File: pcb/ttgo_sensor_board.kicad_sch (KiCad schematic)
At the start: 59 parts, among them J1 Conn_01x13_Female, J2 Conn_01x13_Female, J3 Conn_01x03_Female, J4 Conn_01x03_Female, J5 Conn_01x04_Female, J6 Conn_01x04_Female, J7 Conn_01x04_Female, Q1 Q_NMOS_GSD, Q2 Q_NMOS_GSD, U1 BME680, U2 TCA9800, U3 TLV70218_SOT23-5, U4 LSM6DS3, U5 VEML7700

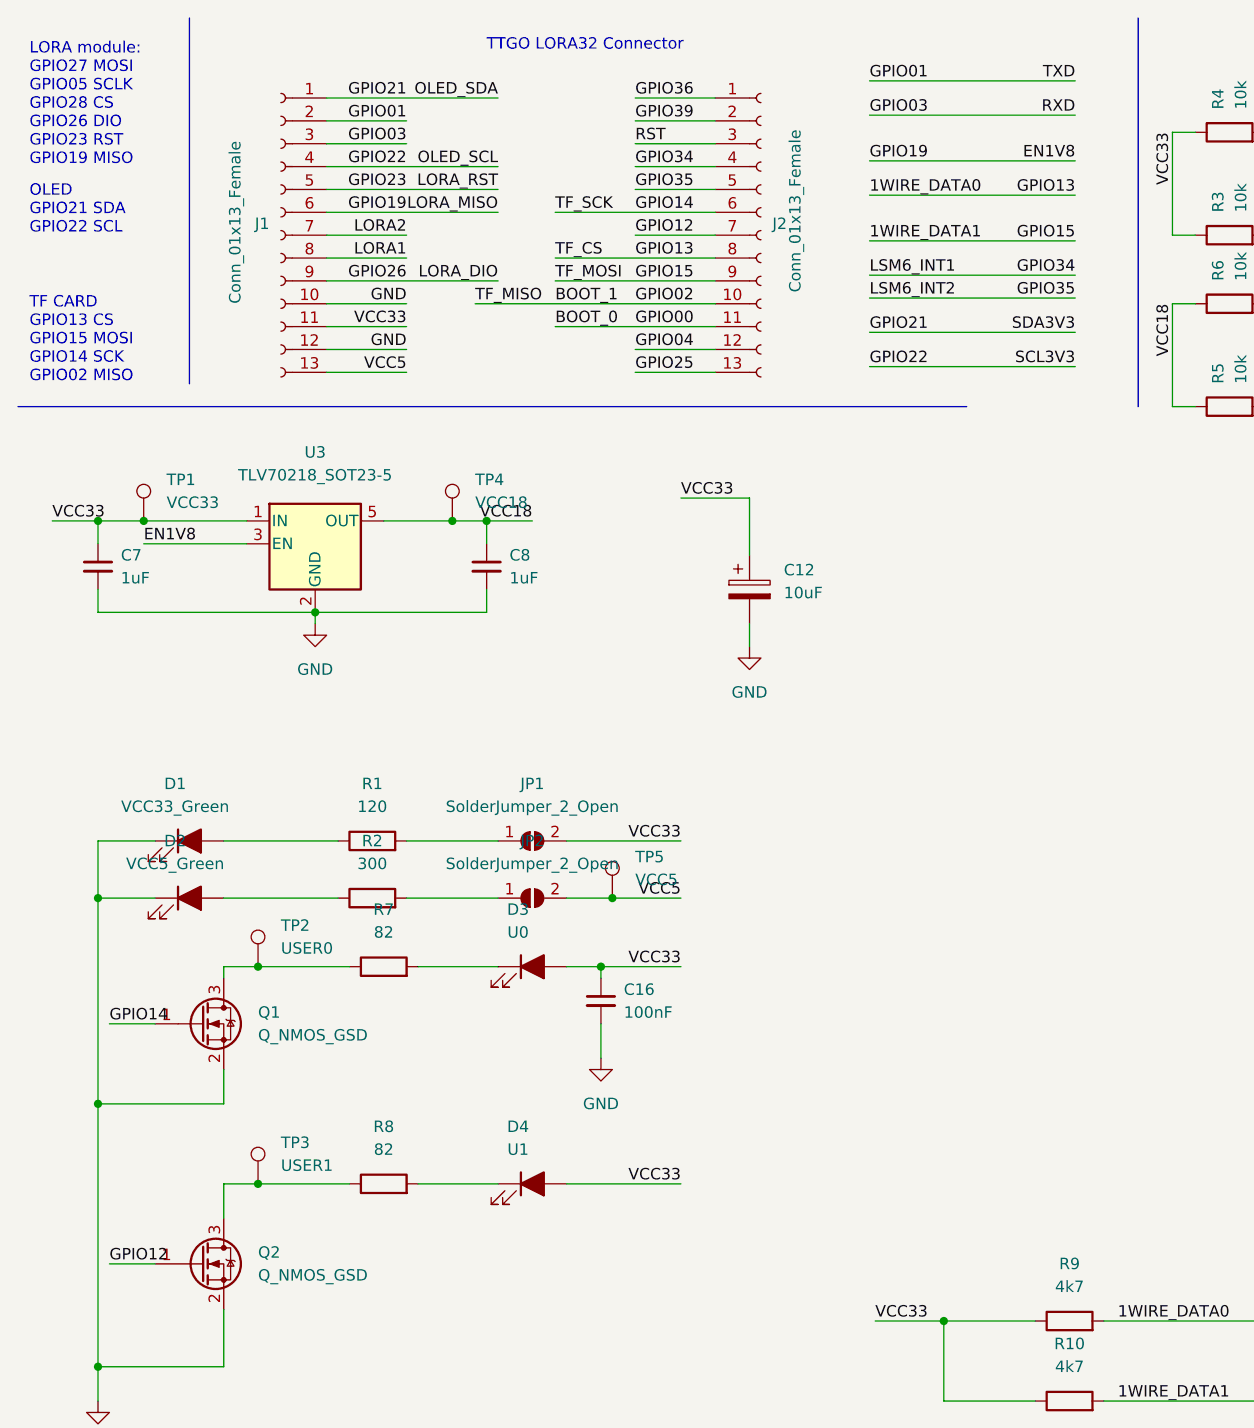
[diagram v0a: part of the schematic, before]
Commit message: update schematic
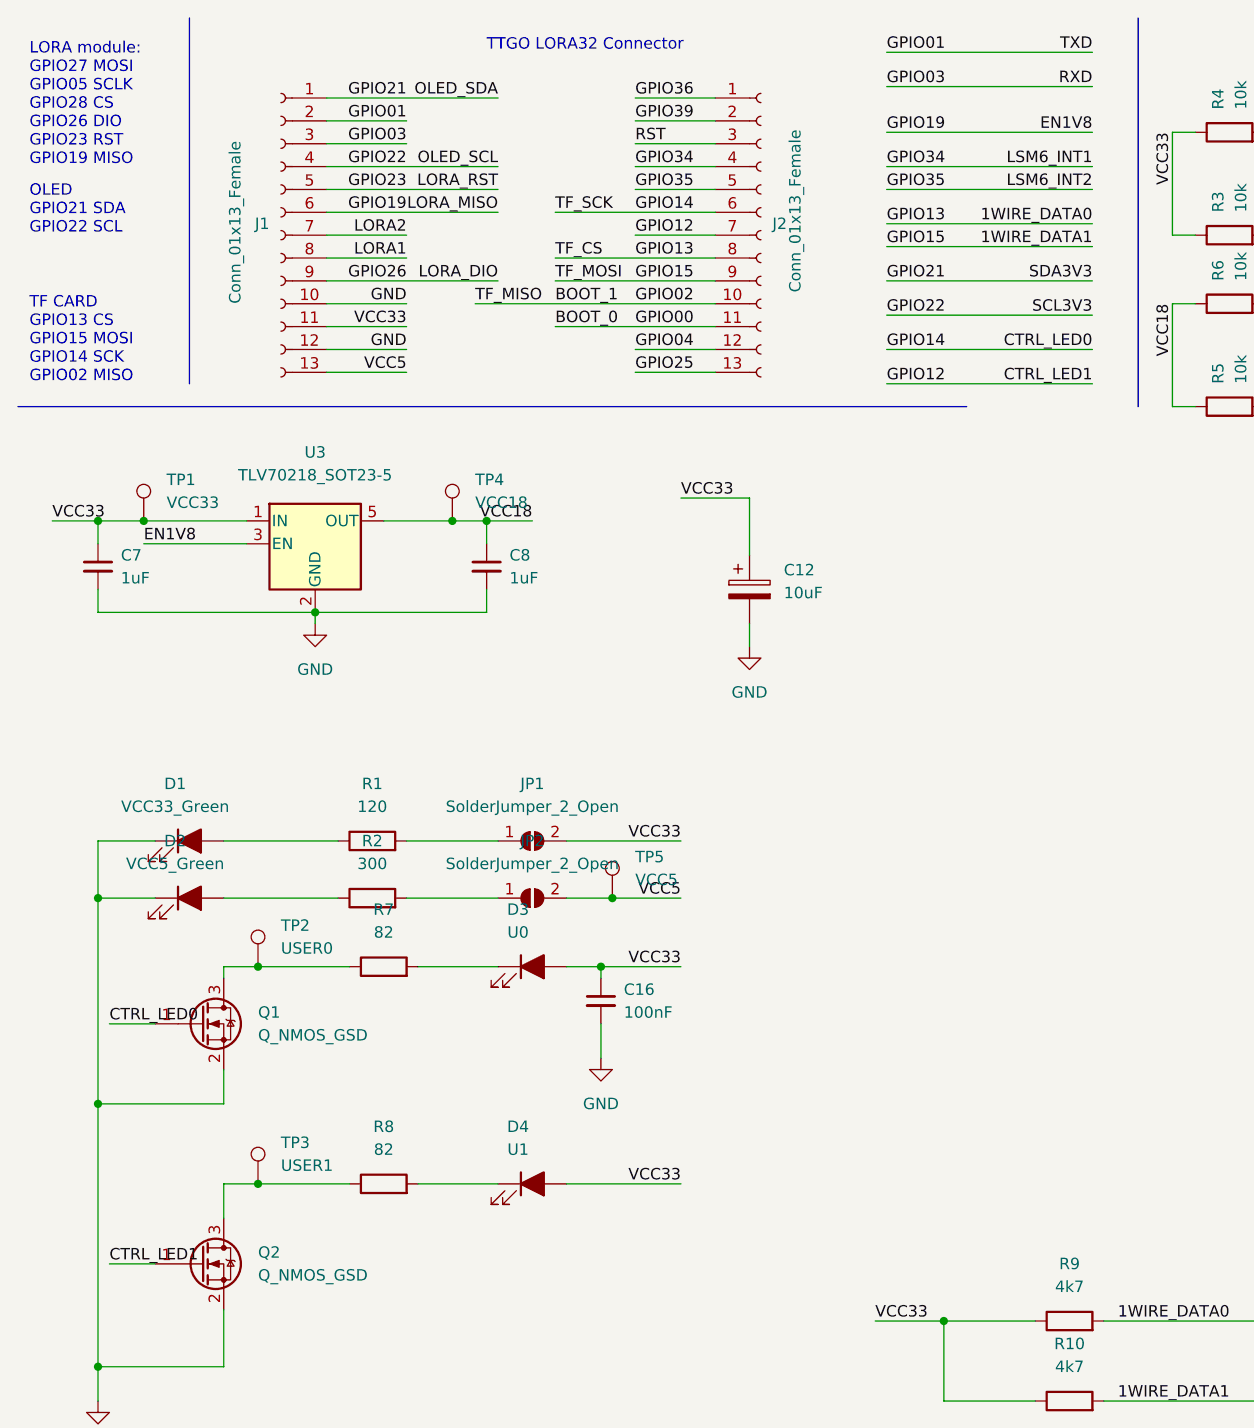
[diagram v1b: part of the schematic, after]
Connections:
- net GPIO12 renamed CTRL_LED1
- net GPIO14 renamed CTRL_LED0
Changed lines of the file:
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@@
     (stroke (width 0) (type default))
   )
-  (wire (pts (xy 108.585 32.385) (xy 131.445 32.385))
+  (wire (pts (xy 133.35 35.56) (xy 110.49 35.56))
+    (stroke (width 0) (type default))
+  )
+  (wire (pts (xy 110.49 49.53) (xy 133.35 49.53))
     (stroke (width 0) (type default))
   )
@@
     (stroke (width 0) (type default))
   )
-  (wire (pts (xy 108.585 41.275) (xy 131.445 41.275))
+  (wire (pts (xy 133.35 29.21) (xy 110.49 29.21))
     (stroke (width 0) (type default))
   )
@@
     (stroke (width 0) (type default))
   )
+  (wire (pts (xy 110.49 53.34) (xy 133.35 53.34))
+    (stroke (width 0) (type default))
+  )
   (wire (pts (xy 22.86 104.14) (xy 22.86 110.49))
     (stroke (width 0) (type default))
@@
     (stroke (width 0) (type default))
   )
-  (wire (pts (xy 108.585 47.625) (xy 131.445 47.625))
+  (wire (pts (xy 110.49 41.91) (xy 133.35 41.91))
     (stroke (width 0) (type default))
   )
@@
     (stroke (width 0) (type default))
   )
-  (wire (pts (xy 108.585 23.495) (xy 131.445 23.495))
+  (wire (pts (xy 110.49 20.32) (xy 133.35 20.32))
     (stroke (width 0) (type default))
   )
@@
     (stroke (width 0) (type default))
   )
-  (wire (pts (xy 108.585 19.685) (xy 131.445 19.685))
+  (wire (pts (xy 110.49 16.51) (xy 133.35 16.51))
     (stroke (width 0) (type default))
   )
@@
     (stroke (width 0) (type default))
   )
-  (wire (pts (xy 108.585 51.435) (xy 131.445 51.435))
+  (wire (pts (xy 110.49 45.72) (xy 133.35 45.72))
     (stroke (width 0) (type default))
   )
@@
     (stroke (width 0) (type default))
   )
-  (wire (pts (xy 108.585 37.465) (xy 131.445 37.465))
+  (wire (pts (xy 133.35 38.1) (xy 110.49 38.1))
     (stroke (width 0) (type default))
   )
@@
     (stroke (width 0) (type default))
   )
-  (wire (pts (xy 108.585 28.575) (xy 131.445 28.575))
+  (wire (pts (xy 110.49 25.4) (xy 133.35 25.4))
     (stroke (width 0) (type default))
   )
@@
     (stroke (width 0) (type default))
   )
-  (wire (pts (xy 108.585 43.815) (xy 131.445 43.815))
+  (wire (pts (xy 133.35 31.75) (xy 110.49 31.75))
     (stroke (width 0) (type default))
   )
@@
     (effects (font (size 1.27 1.27)) (justify left bottom))
   )
-  (label "1WIRE_DATA1" (at 108.585 37.465 0) (fields_autoplaced)
-    (effects (font (size 1.27 1.27)) (justify left bottom))
+  (label "1WIRE_DATA1" (at 133.35 38.1 180) (fields_autoplaced)
+    (effects (font (size 1.27 1.27)) (justify right bottom))
   )
   (label "GPIO14" (at 82.55 34.29 0) (fields_autoplaced)
@@
     (effects (font (size 1.27 1.27)) (justify right bottom))
   )
+  (label "GPIO14" (at 110.49 49.53 0) (fields_autoplaced)
+    (effects (font (size 1.27 1.27)) (justify left bottom))
+  )
   (label "SDA3V3" (at 161.29 36.83 180) (fields_autoplaced)
     (effects (font (size 1.27 1.27)) (justify right bottom))
@@
     (effects (font (size 1.27 1.27)) (justify right bottom))
   )
-  (label "LSM6_INT2" (at 108.585 43.815 0) (fields_autoplaced)
-    (effects (font (size 1.27 1.27)) (justify left bottom))
+  (label "LSM6_INT2" (at 133.35 31.75 180) (fields_autoplaced)
+    (effects (font (size 1.27 1.27)) (justify right bottom))
   )
   (label "GPIO22" (at 57.15 29.21 180) (fields_autoplaced)
     (effects (font (size 1.27 1.27)) (justify right bottom))
   )
-  (label "TXD" (at 131.445 19.685 180) (fields_autoplaced)
+  (label "TXD" (at 133.35 16.51 180) (fields_autoplaced)
     (effects (font (size 1.27 1.27)) (justify right bottom))
   )
@@
     (effects (font (size 1.27 1.27)) (justify left bottom))
   )
-  (label "GPIO03" (at 108.585 23.495 0) (fields_autoplaced)
-    (effects (font (size 1.27 1.27)) (justify left bottom))
-  )
-  (label "GPIO34" (at 131.445 41.275 180) (fields_autoplaced)
-    (effects (font (size 1.27 1.27)) (justify right bottom))
+  (label "CTRL_LED1" (at 133.35 53.34 180) (fields_autoplaced)
+    (effects (font (size 1.27 1.27)) (justify right bottom))
+  )
+  (label "GPIO03" (at 110.49 20.32 0) (fields_autoplaced)
+    (effects (font (size 1.27 1.27)) (justify left bottom))
+  )
+  (label "GPIO34" (at 110.49 29.21 0) (fields_autoplaced)
+    (effects (font (size 1.27 1.27)) (justify left bottom))
   )
   (label "VCC33" (at 17.78 68.58 0) (fields_autoplaced)
@@
     (effects (font (size 1.27 1.27)) (justify left bottom))
   )
+  (label "CTRL_LED0" (at 133.35 49.53 180) (fields_autoplaced)
+    (effects (font (size 1.27 1.27)) (justify right bottom))
+  )
   (label "VCC33" (at 213.36 20.32 180) (fields_autoplaced)
     (effects (font (size 1.27 1.27)) (justify right bottom))
@@
     (effects (font (size 1.27 1.27)) (justify right bottom))
   )
-  (label "1WIRE_DATA0" (at 108.585 32.385 0) (fields_autoplaced)
-    (effects (font (size 1.27 1.27)) (justify left bottom))
+  (label "1WIRE_DATA0" (at 133.35 35.56 180) (fields_autoplaced)
+    (effects (font (size 1.27 1.27)) (justify right bottom))
   )
   (label "GPIO39" (at 82.55 24.13 0) (fields_autoplaced)
     (effects (font (size 1.27 1.27)) (justify left bottom))
   )
-  (label "GPIO13" (at 131.445 32.385 180) (fields_autoplaced)
-    (effects (font (size 1.27 1.27)) (justify right bottom))
+  (label "GPIO13" (at 110.49 35.56 0) (fields_autoplaced)
+    (effects (font (size 1.27 1.27)) (justify left bottom))
   )
   (label "VCC18" (at 71.12 68.58 180) (fields_autoplaced)
@@
     (effects (font (size 1.27 1.27)) (justify left bottom))
   )
-  (label "EN1V8" (at 131.445 28.575 180) (fields_autoplaced)
+  (label "EN1V8" (at 133.35 25.4 180) (fields_autoplaced)
     (effects (font (size 1.27 1.27)) (justify right bottom))
   )
@@
     (effects (font (size 1.27 1.27)) (justify right bottom))
   )
-  (label "SCL3V3" (at 131.445 51.435 180) (fields_autoplaced)
+  (label "SCL3V3" (at 133.35 45.72 180) (fields_autoplaced)
     (effects (font (size 1.27 1.27)) (justify right bottom))
   )
@@
     (effects (font (size 1.27 1.27)) (justify left bottom))
   )
-  (label "GPIO01" (at 108.585 19.685 0) (fields_autoplaced)
+  (label "GPIO01" (at 110.49 16.51 0) (fields_autoplaced)
     (effects (font (size 1.27 1.27)) (justify left bottom))
   )
@@
     (effects (font (size 1.27 1.27)) (justify left bottom))
   )
-  (label "SDA3V3" (at 131.445 47.625 180) (fields_autoplaced)
+  (label "SDA3V3" (at 133.35 41.91 180) (fields_autoplaced)
     (effects (font (size 1.27 1.27)) (justify right bottom))
   )
@@
     (effects (font (size 1.27 1.27)) (justify left bottom))
   )
-  (label "GPIO35" (at 131.445 43.815 180) (fields_autoplaced)
-    (effects (font (size 1.27 1.27)) (justify right bottom))
+  (label "GPIO35" (at 110.49 31.75 0) (fields_autoplaced)
+    (effects (font (size 1.27 1.27)) (justify left bottom))
   )
   (label "LORA_MISO" (at 67.31 34.29 180) (fields_autoplaced)
@@
     (effects (font (size 1.27 1.27)) (justify right bottom))
   )
+  (label "GPIO12" (at 110.49 53.34 0) (fields_autoplaced)
+    (effects (font (size 1.27 1.27)) (justify left bottom))
+  )
   (label "RST" (at 82.55 26.67 0) (fields_autoplaced)
     (effects (font (size 1.27 1.27)) (justify left bottom))
@@
     (effects (font (size 1.27 1.27)) (justify left bottom))
   )
-  (label "RXD" (at 131.445 23.495 180) (fields_autoplaced)
+  (label "RXD" (at 133.35 20.32 180) (fields_autoplaced)
     (effects (font (size 1.27 1.27)) (justify right bottom))
   )
@@
     (effects (font (size 1.27 1.27)) (justify left bottom))
   )
-  (label "GPIO19" (at 108.585 28.575 0) (fields_autoplaced)
+  (label "GPIO19" (at 110.49 25.4 0) (fields_autoplaced)
     (effects (font (size 1.27 1.27)) (justify left bottom))
   )
@@
     (effects (font (size 1.27 1.27)) (justify left bottom))
   )
-  (label "GPIO12" (at 24.13 151.13 0) (fields_autoplaced)
+  (label "CTRL_LED1" (at 24.13 151.13 0) (fields_autoplaced)
     (effects (font (size 1.27 1.27)) (justify left bottom))
   )
@@
     (effects (font (size 1.27 1.27)) (justify right bottom))
   )
-  (label "GPIO21" (at 108.585 47.625 0) (fields_autoplaced)
-    (effects (font (size 1.27 1.27)) (justify left bottom))
-  )
-  (label "GPIO22" (at 108.585 51.435 0) (fields_autoplaced)
+  (label "GPIO21" (at 110.49 41.91 0) (fields_autoplaced)
+    (effects (font (size 1.27 1.27)) (justify left bottom))
+  )
+  (label "GPIO22" (at 110.49 45.72 0) (fields_autoplaced)
     (effects (font (size 1.27 1.27)) (justify left bottom))
   )
@@
     (effects (font (size 1.27 1.27)) (justify right bottom))
   )
-  (label "GPIO15" (at 131.445 37.465 180) (fields_autoplaced)
-    (effects (font (size 1.27 1.27)) (justify right bottom))
-  )
-  (label "LSM6_INT1" (at 108.585 41.275 0) (fields_autoplaced)
-    (effects (font (size 1.27 1.27)) (justify left bottom))
-  )
-  (label "GPIO14" (at 24.13 124.46 0) (fields_autoplaced)
-    (effects (font (size 1.27 1.27)) (justify left bottom))
-  )
+  (label "GPIO15" (at 110.49 38.1 0) (fields_autoplaced)
+    (effects (font (size 1.27 1.27)) (justify left bottom))
+  )
+  (label "LSM6_INT1" (at 133.35 29.21 180) (fields_autoplaced)
+    (effects (font (size 1.27 1.27)) (justify right bottom))
+  )
+  (label "CTRL_LED0" (at 24.13 124.46 0) (fields_autoplaced)
+    (effects (font (size 1.27 1.27)) (justify left bottom))
+  )
